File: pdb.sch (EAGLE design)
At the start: 42 parts, among them Q1 20MHz, Q2 IRFR5305PBF, Q3 IRFR5305PBF, U1 TSR_1-2433, U2 LTC2946CMSPBF, U3 LTC2946CMSPBF, U4 LTC2946CMSPBF, U5 ATMEGA48-20AU, U6 TXB0104, U7 AT30TS74SS8M

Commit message: wip
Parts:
- removed BAT: XT60PWMALE, amass:XT60PWMALE
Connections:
- removed net N$3: BAT.+, Q2.D
- new net BAT_IN: Q2.D
- net GND: no longer BAT.-
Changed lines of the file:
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@@
 <part name="U1" library="Robo-Lib" deviceset="TSR_1-*" device="" technology="2433"/>
 <part name="SUPPLY6" library="supply2" library_urn="urn:adsk.eagle:library:372" deviceset="V+" device=""/>
-<part name="BAT" library="amass" library_urn="urn:adsk.eagle:library:538876" deviceset="XT60PW" device="MALE" package3d_urn="urn:adsk.eagle:package:538884/2"/>
 <part name="LED1" library="led" library_urn="urn:adsk.eagle:library:259" deviceset="LED" device="CHIP-LED0603" package3d_urn="urn:adsk.eagle:package:15819/3" value="blau"/>
 <part name="LED2" library="led" library_urn="urn:adsk.eagle:library:259" deviceset="LED" device="CHIP-LED0603" package3d_urn="urn:adsk.eagle:package:15819/3" value="grün"/>
@@
 <instance part="U1" gate="G$1" x="2.54" y="15.24"/>
 <instance part="SUPPLY6" gate="1" x="-12.7" y="20.32"/>
-<instance part="BAT" gate="G$1" x="-99.06" y="53.34" rot="MR0"/>
 <instance part="R4" gate="G$1" x="-27.94" y="55.88"/>
 <instance part="R5" gate="G$1" x="25.4" y="55.88"/>
@@
 <wire x1="-81.28" y1="50.8" x2="-81.28" y2="48.26" width="0.1524" layer="91"/>
 <pinref part="GND25" gate="1" pin="GND"/>
-<pinref part="BAT" gate="G$1" pin="-"/>
 </segment>
 <segment>
@@
 </segment>
 </net>
-<net name="AKKU-ZWISCHEN" class="2">
+<net name="AKKU-ZWISCHEN" class="1">
 <segment>
 <pinref part="Q2" gate="G$1" pin="S"/>
@@
 </segment>
 </net>
-<net name="N$3" class="0">
+<net name="BAT_IN" class="1">
 <segment>
 <pinref part="Q2" gate="G$1" pin="D"/>
 <wire x1="-88.9" y1="55.88" x2="-78.74" y2="55.88" width="0.1524" layer="91"/>
-<pinref part="BAT" gate="G$1" pin="+"/>
 </segment>
 </net>
@@
 </segment>
 </net>
-<net name="SENSE+V+" class="3">
+<net name="SENSE+V+" class="4">
 <segment>
 <pinref part="Q3" gate="G$1" pin="D"/>
@@
 </segment>
 </net>
-<net name="SENSE+V+" class="3">
+<net name="SENSE+V+" class="4">
 <segment>
 <pinref part="U2" gate="A" pin="SENSE+"/>

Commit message: changed R6
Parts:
- R6: value CSS2H-3920 -> CRA2512-FZ-R040ELF; device jonas_resistor:CSS2H-3920 -> jonas_bourns:CRA2512-FZ-R040ELF
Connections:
- net +3V3: now also R6.22; no longer R6.2
- net SENSE+3V3: now also R6.11; no longer R6.1
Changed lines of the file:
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@@
 <?xml version="1.0" encoding="utf-8"?>
 <!DOCTYPE eagle SYSTEM "eagle.dtd">
-<eagle version="8.5.2">
+<eagle version="8.6.0">
 <drawing>
 <settings>
@@
 <part name="R4" library="jonas_resistor" library_urn="urn:adsk.eagle:library:539632" deviceset="CSS2H-3920" device="" package3d_urn="urn:adsk.eagle:package:539635/1"/>
 <part name="R5" library="jonas_resistor" library_urn="urn:adsk.eagle:library:539632" deviceset="CSS2H-3920" device="" package3d_urn="urn:adsk.eagle:package:539635/1"/>
-<part name="R6" library="jonas_resistor" library_urn="urn:adsk.eagle:library:539632" deviceset="CSS2H-3920" device="" package3d_urn="urn:adsk.eagle:package:539635/1"/>
 <part name="+3V3" library="supply1" library_urn="urn:adsk.eagle:library:371" deviceset="+3V3" device=""/>
 <part name="SUPPLY12" library="supply2" library_urn="urn:adsk.eagle:library:372" deviceset="+5V" device=""/>
@@
 <part name="GND22" library="supply1" library_urn="urn:adsk.eagle:library:371" deviceset="GND" device=""/>
 <part name="SUPPLY21" library="supply2" deviceset="+5V" device=""/>
+<part name="R6" library="jonas_bourns" library_urn="urn:adsk.eagle:library:1422904" deviceset="CRA2512-FZ-R040ELF" device="" package3d_urn="urn:adsk.eagle:package:1633525/2"/>
 </parts>
 <sheets>
@@
 <instance part="GND19" gate="1" x="38.1" y="0"/>
 <instance part="GND15" gate="1" x="15.24" y="2.54"/>
-<instance part="+3V2" gate="G$1" x="53.34" y="20.32"/>
+<instance part="+3V2" gate="G$1" x="58.42" y="20.32"/>
 <instance part="U1" gate="G$1" x="2.54" y="15.24"/>
 <instance part="SUPPLY6" gate="1" x="-12.7" y="20.32"/>
 <instance part="R4" gate="G$1" x="-27.94" y="55.88"/>
 <instance part="R5" gate="G$1" x="25.4" y="55.88"/>
-<instance part="R6" gate="G$1" x="45.72" y="15.24"/>
 <instance part="FRAME3" gate="G$1" x="-127" y="-50.8"/>
 <instance part="ESC" gate="G$1" x="-99.06" y="-17.78" rot="MR0"/>
@@
 <instance part="SUPPLY17" gate="1" x="-86.36" y="-10.16"/>
 <instance part="L2" gate="A" x="20.32" y="15.24"/>
+<instance part="R6" gate="A" x="43.18" y="15.24"/>
 </instances>
 <busses>
@@
 <wire x1="38.1" y1="15.24" x2="38.1" y2="12.7" width="0.1524" layer="91"/>
 <pinref part="C4" gate="G$1" pin="1"/>
-<pinref part="R6" gate="G$1" pin="1"/>
-<wire x1="38.1" y1="15.24" x2="40.64" y2="15.24" width="0.1524" layer="91"/>
+<wire x1="38.1" y1="15.24" x2="43.18" y2="15.24" width="0.1524" layer="91"/>
 <wire x1="35.56" y1="15.24" x2="38.1" y2="15.24" width="0.1524" layer="91"/>
 <junction x="38.1" y="15.24"/>
@@
 <label x="38.1" y="17.78" size="1.778" layer="95" rot="R90" xref="yes"/>
 <pinref part="L2" gate="A" pin="1"/>
+<pinref part="R6" gate="A" pin="11"/>
 </segment>
 </net>
 <net name="+3V3" class="4">
 <segment>
-<pinref part="R6" gate="G$1" pin="2"/>
-<wire x1="50.8" y1="15.24" x2="53.34" y2="15.24" width="0.1524" layer="91"/>
-<wire x1="53.34" y1="15.24" x2="53.34" y2="17.78" width="0.1524" layer="91"/>
+<wire x1="55.88" y1="15.24" x2="58.42" y2="15.24" width="0.1524" layer="91"/>
+<wire x1="58.42" y1="15.24" x2="58.42" y2="17.78" width="0.1524" layer="91"/>
 <pinref part="+3V2" gate="G$1" pin="+3V3"/>
-</segment>
-</net>
+<pinref part="R6" gate="A" pin="22"/>
+</segment>
+</net>

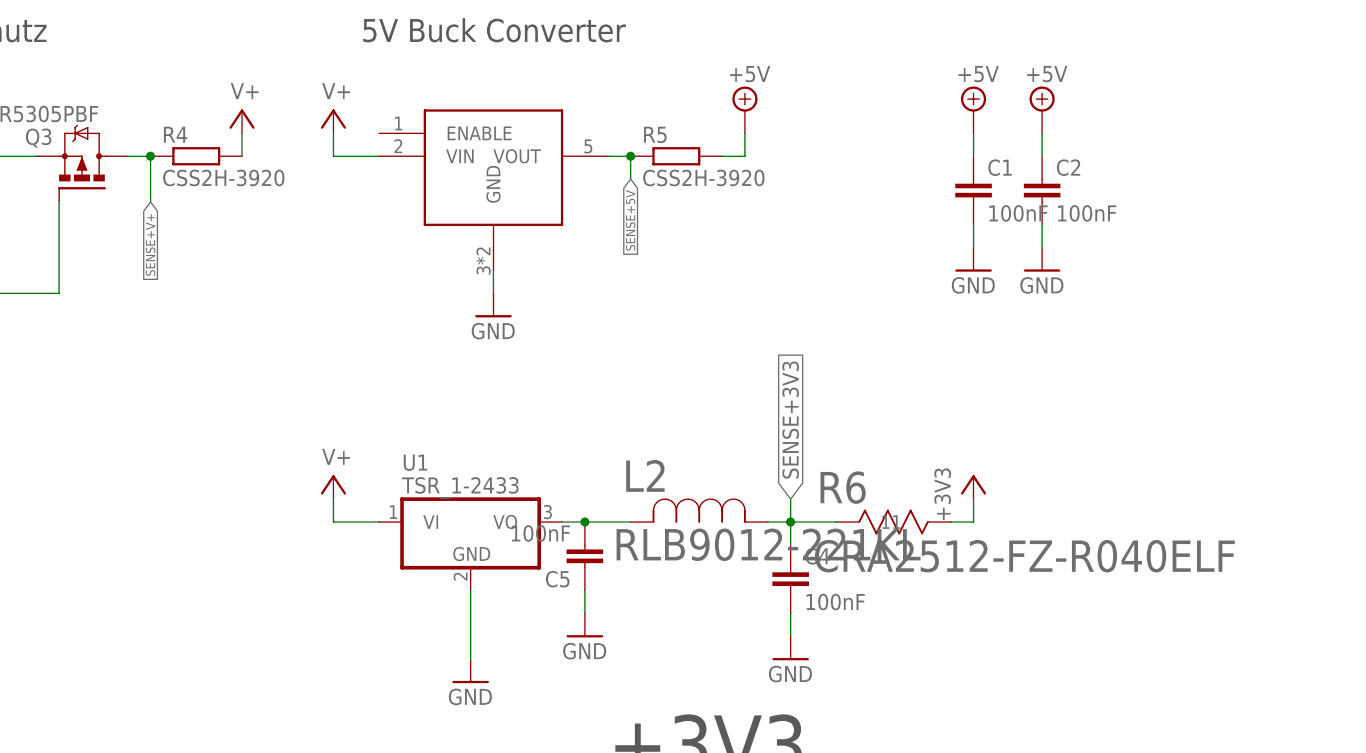
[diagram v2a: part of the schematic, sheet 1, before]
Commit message: fixed shunt resistor libraries
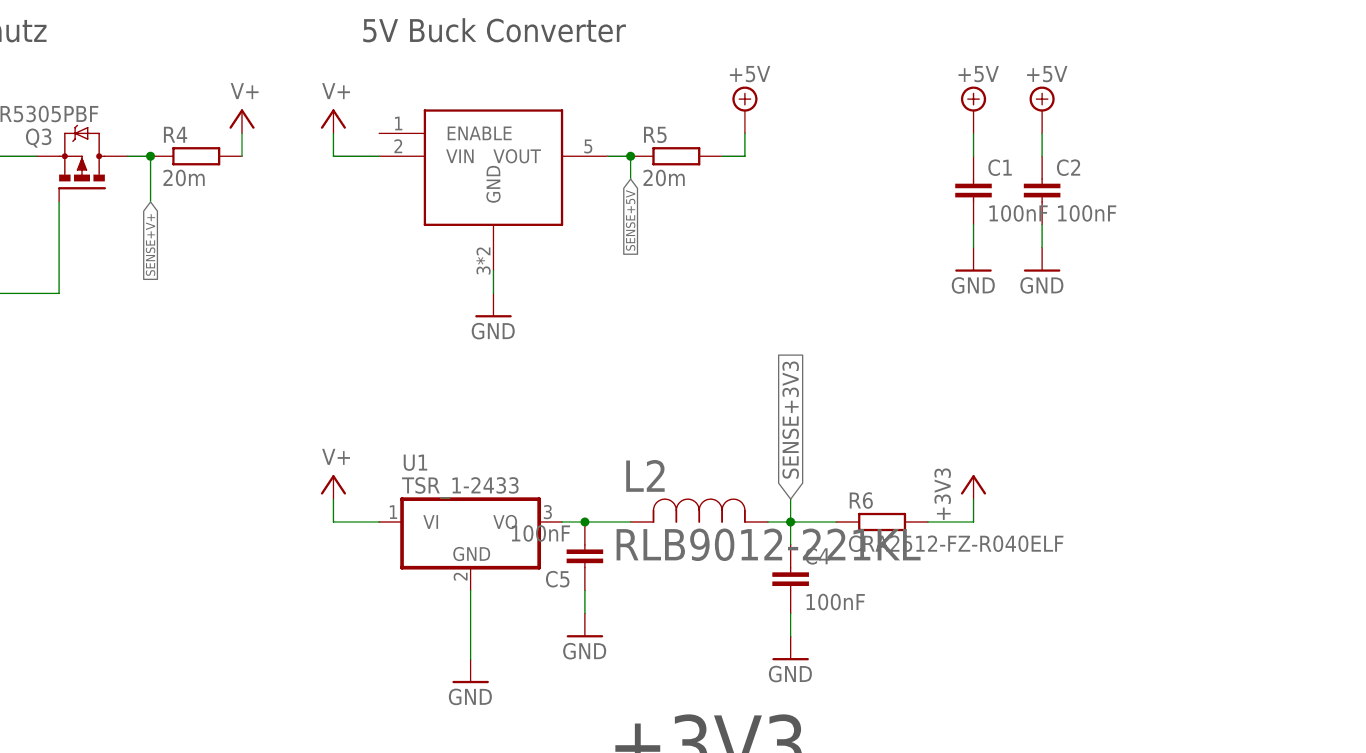
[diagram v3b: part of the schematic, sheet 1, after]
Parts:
- R4, R5: value CSS2H-3920 -> 20m
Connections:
- net +3V3: now also R6.2; no longer R6.22
- net SENSE+3V3: now also R6.1; no longer R6.11
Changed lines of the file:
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@@
 <layer number="97" name="Info" color="7" fill="1" visible="yes" active="yes"/>
 <layer number="98" name="Guide" color="6" fill="1" visible="yes" active="yes"/>
-<layer number="99" name="SpiceOrder" color="7" fill="1" visible="yes" active="yes"/>
+<layer number="99" name="SpiceOrder" color="7" fill="1" visible="no" active="yes"/>
 <layer number="100" name="Muster" color="7" fill="1" visible="no" active="no"/>
 <layer number="101" name="Hidden" color="15" fill="1" visible="yes" active="yes"/>
@@
 <part name="SUPPLY10" library="supply2" library_urn="urn:adsk.eagle:library:372" deviceset="V+" device=""/>
 <part name="SUPPLY11" library="supply2" library_urn="urn:adsk.eagle:library:372" deviceset="V+" device=""/>
-<part name="R4" library="jonas_resistor" library_urn="urn:adsk.eagle:library:539632" deviceset="CSS2H-3920" device="" package3d_urn="urn:adsk.eagle:package:539635/1"/>
-<part name="R5" library="jonas_resistor" library_urn="urn:adsk.eagle:library:539632" deviceset="CSS2H-3920" device="" package3d_urn="urn:adsk.eagle:package:539635/1"/>
+<part name="R4" library="jonas_resistor" library_urn="urn:adsk.eagle:library:539632" deviceset="CSS2H-3920" device="" package3d_urn="urn:adsk.eagle:package:539635/1" value="20m"/>
+<part name="R5" library="jonas_resistor" library_urn="urn:adsk.eagle:library:539632" deviceset="CSS2H-3920" device="" package3d_urn="urn:adsk.eagle:package:539635/1" value="20m"/>
 <part name="+3V3" library="supply1" library_urn="urn:adsk.eagle:library:371" deviceset="+3V3" device=""/>
 <part name="SUPPLY12" library="supply2" library_urn="urn:adsk.eagle:library:372" deviceset="+5V" device=""/>
@@
 <instance part="SUPPLY17" gate="1" x="-86.36" y="-10.16"/>
 <instance part="L2" gate="A" x="20.32" y="15.24"/>
-<instance part="R6" gate="A" x="43.18" y="15.24"/>
+<instance part="R6" gate="G$1" x="48.26" y="15.24"/>
 </instances>
 <busses>
@@
 <wire x1="38.1" y1="15.24" x2="38.1" y2="12.7" width="0.1524" layer="91"/>
 <pinref part="C4" gate="G$1" pin="1"/>
-<wire x1="38.1" y1="15.24" x2="43.18" y2="15.24" width="0.1524" layer="91"/>
 <wire x1="35.56" y1="15.24" x2="38.1" y2="15.24" width="0.1524" layer="91"/>
 <junction x="38.1" y="15.24"/>
@@
 <label x="38.1" y="17.78" size="1.778" layer="95" rot="R90" xref="yes"/>
 <pinref part="L2" gate="A" pin="1"/>
-<pinref part="R6" gate="A" pin="11"/>
+<pinref part="R6" gate="G$1" pin="1"/>
+<wire x1="38.1" y1="15.24" x2="43.18" y2="15.24" width="0.1524" layer="91"/>
 </segment>
 </net>
 <net name="+3V3" class="4">
 <segment>
-<wire x1="55.88" y1="15.24" x2="58.42" y2="15.24" width="0.1524" layer="91"/>
 <wire x1="58.42" y1="15.24" x2="58.42" y2="17.78" width="0.1524" layer="91"/>
 <pinref part="+3V2" gate="G$1" pin="+3V3"/>
-<pinref part="R6" gate="A" pin="22"/>
-</segment>
-</net>
+<pinref part="R6" gate="G$1" pin="2"/>
+<wire x1="53.34" y1="15.24" x2="58.42" y2="15.24" width="0.1524" layer="91"/>
+</segment>
+</net>

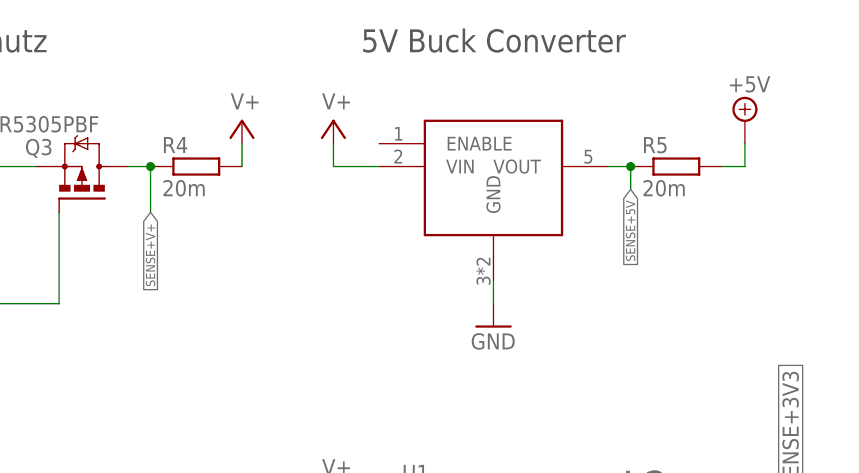
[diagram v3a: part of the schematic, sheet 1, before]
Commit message: fixed shunt resistor value
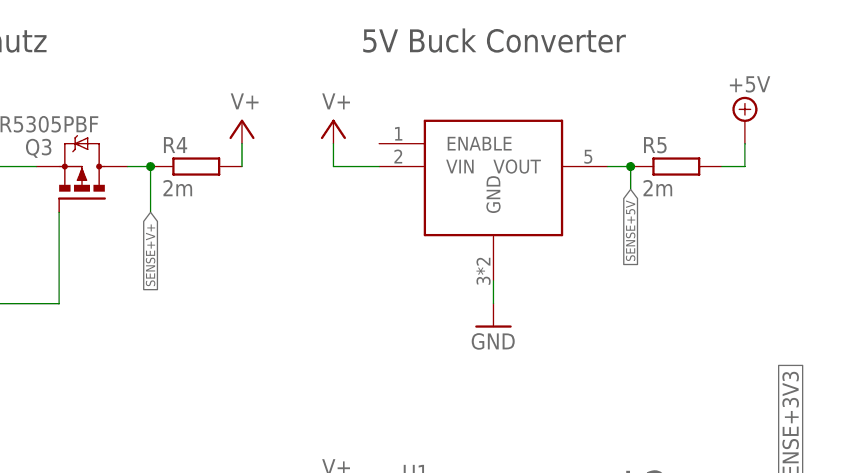
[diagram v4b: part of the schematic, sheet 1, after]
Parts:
- R4, R5: value 20m -> 2m
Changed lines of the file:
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@@
 <part name="SUPPLY10" library="supply2" library_urn="urn:adsk.eagle:library:372" deviceset="V+" device=""/>
 <part name="SUPPLY11" library="supply2" library_urn="urn:adsk.eagle:library:372" deviceset="V+" device=""/>
-<part name="R4" library="jonas_resistor" library_urn="urn:adsk.eagle:library:539632" deviceset="CSS2H-3920" device="" package3d_urn="urn:adsk.eagle:package:539635/1" value="20m"/>
-<part name="R5" library="jonas_resistor" library_urn="urn:adsk.eagle:library:539632" deviceset="CSS2H-3920" device="" package3d_urn="urn:adsk.eagle:package:539635/1" value="20m"/>
+<part name="R4" library="jonas_resistor" library_urn="urn:adsk.eagle:library:539632" deviceset="CSS2H-3920" device="" package3d_urn="urn:adsk.eagle:package:539635/1" value="2m"/>
+<part name="R5" library="jonas_resistor" library_urn="urn:adsk.eagle:library:539632" deviceset="CSS2H-3920" device="" package3d_urn="urn:adsk.eagle:package:539635/1" value="2m"/>
 <part name="+3V3" library="supply1" library_urn="urn:adsk.eagle:library:371" deviceset="+3V3" device=""/>
 <part name="SUPPLY12" library="supply2" library_urn="urn:adsk.eagle:library:372" deviceset="+5V" device=""/>

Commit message: various improvements/fixes
added power output pins
fixed design rules
moved ESC out to bottom
fixed packages
removed unnecessary filtering for atmega
etc
(may be more but that was last week i don't remember anymore)
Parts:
- removed C10: 100nF, resistor:C-EUC1206
- removed L1: 100µH, rcl:L-EU0204/7
- added JP10, JP2, JP3, JP4, JP5, JP6, JP7, JP8, JP9: (no value), pinhead:PINHD-1X2
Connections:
- removed net N$88: C10.2, L1.1, U5B.AVCC
- net +3V3: now also JP10.1, JP8.1, JP9.1
- net +5V: now also JP5.1, JP6.1, JP7.1, U5B.AVCC; no longer L1.2
- net GND: now also JP10.2, JP2.2, JP3.2, JP4.2, JP5.2, JP6.2, JP7.2, JP8.2, JP9.2; no longer C10.1
- net V+: now also JP2.1, JP3.1, JP4.1
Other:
- note removed: "TODO: Replace with SMT package"

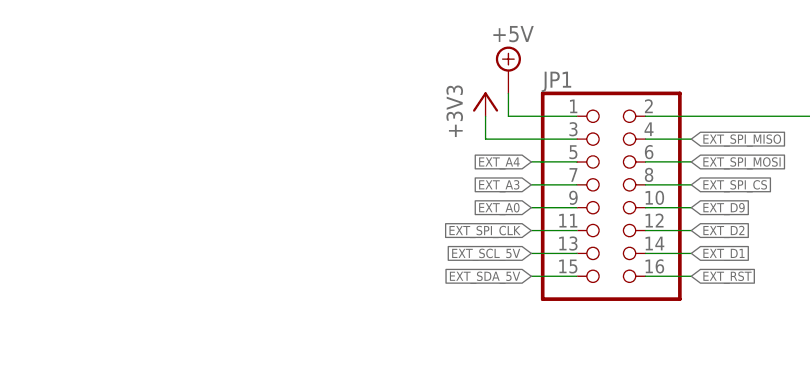
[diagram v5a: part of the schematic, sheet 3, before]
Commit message: fixed #10
removed expansion port connections
rotated expansion port
connected expansion port
added 3V3 jumper
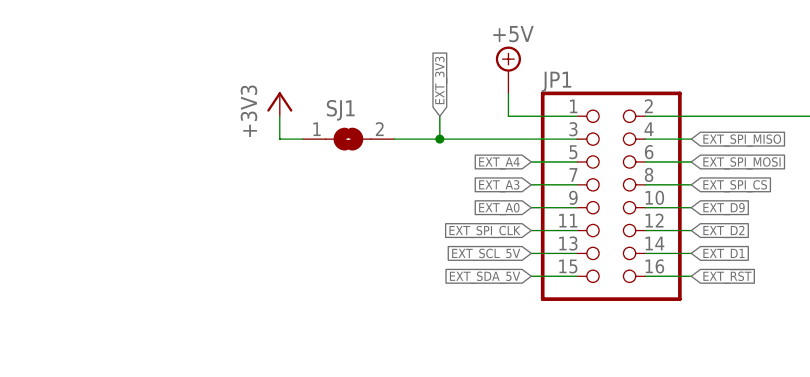
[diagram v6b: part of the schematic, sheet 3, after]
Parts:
- added SJ1: (no value), jumper:SJ
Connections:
- new net EXT_3V3: JP1.3, SJ1.2, U6.VCCA
- net +3V3: now also SJ1.1; no longer JP1.3, U6.VCCA
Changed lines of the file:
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@@
 <part name="SUPPLY16" library="supply2" deviceset="+5V" device=""/>
 <part name="GND16" library="supply1" deviceset="GND" device=""/>
-<part name="+3V4" library="supply1" library_urn="urn:adsk.eagle:library:371" deviceset="+3V3" device=""/>
 <part name="ESC" library="amass" library_urn="urn:adsk.eagle:library:538876" deviceset="XT60PW" device="FEMALE" package3d_urn="urn:adsk.eagle:package:538883/2" value="XT60PWFEMALE"/>
 <part name="GND18" library="supply1" deviceset="GND" device=""/>
@@
 <part name="GND21" library="supply1" library_urn="urn:adsk.eagle:library:371" deviceset="GND" device=""/>
 <part name="SUPPLY19" library="supply2" library_urn="urn:adsk.eagle:library:372" deviceset="+5V" device=""/>
-<part name="+3V5" library="supply1" library_urn="urn:adsk.eagle:library:371" deviceset="+3V3" device=""/>
 <part name="R7" library="rcl" library_urn="urn:adsk.eagle:library:334" deviceset="R-EU_" device="R0805" package3d_urn="urn:adsk.eagle:package:23553/2" value="4,7k"/>
 <part name="R8" library="rcl" library_urn="urn:adsk.eagle:library:334" deviceset="R-EU_" device="R0805" package3d_urn="urn:adsk.eagle:package:23553/2" value="4,7k"/>
@@
 <part name="SUPPLY22" library="supply2" library_urn="urn:adsk.eagle:library:372" deviceset="+5V" device=""/>
 <part name="+3V6" library="supply1" library_urn="urn:adsk.eagle:library:371" deviceset="+3V3" device=""/>
+<part name="SJ1" library="jumper" library_urn="urn:adsk.eagle:library:252" deviceset="SJ" device="" package3d_urn="urn:adsk.eagle:package:15471/1"/>
+<part name="+3V4" library="supply1" library_urn="urn:adsk.eagle:library:371" deviceset="+3V3" device=""/>
 </parts>
 <sheets>
@@
 <instance part="SUPPLY16" gate="+5V" x="45.72" y="106.68"/>
 <instance part="GND16" gate="1" x="40.64" y="63.5"/>
-<instance part="+3V4" gate="G$1" x="35.56" y="106.68"/>
 <instance part="R7" gate="G$1" x="66.04" y="76.2" rot="R180"/>
 <instance part="R8" gate="G$1" x="66.04" y="83.82" rot="R180"/>
@@
 <wire x1="50.8" y1="149.86" x2="50.8" y2="147.32" width="0.1524" layer="91"/>
 </segment>
-<segment>
-<pinref part="U6" gate="G$1" pin="VCCA"/>
-<wire x1="35.56" y1="101.6" x2="35.56" y2="104.14" width="0.1524" layer="91"/>
-<pinref part="+3V4" gate="G$1" pin="+3V3"/>
-</segment>
 </net>
 <net name="+5V" class="4">
@@
 <wire x1="55.88" y1="81.28" x2="60.96" y2="81.28" width="0.1524" layer="91"/>
 <wire x1="60.96" y1="81.28" x2="60.96" y2="76.2" width="0.1524" layer="91"/>
+</segment>
+</net>
+<net name="EXT_3V3" class="4">
+<segment>
+<pinref part="U6" gate="G$1" pin="VCCA"/>
+<wire x1="35.56" y1="101.6" x2="35.56" y2="104.14" width="0.1524" layer="91"/>
+<label x="35.56" y="104.14" size="1.016" layer="95" rot="R90" xref="yes"/>
 </segment>
 </net>
@@
 <instance part="GND21" gate="1" x="180.34" y="213.36"/>
 <instance part="SUPPLY19" gate="+5V" x="142.24" y="223.52"/>
-<instance part="+3V5" gate="G$1" x="139.7" y="220.98"/>
+<instance part="SJ1" gate="1" x="124.46" y="215.9"/>
+<instance part="+3V4" gate="G$1" x="116.84" y="220.98"/>
 </instances>
 <busses>
@@
 </segment>
 <segment>
-<pinref part="JP1" gate="A" pin="3"/>
-<wire x1="149.86" y1="215.9" x2="139.7" y2="215.9" width="0.1524" layer="91"/>
-<wire x1="139.7" y1="215.9" x2="139.7" y2="218.44" width="0.1524" layer="91"/>
-<pinref part="+3V5" gate="G$1" pin="+3V3"/>
+<pinref part="SJ1" gate="1" pin="1"/>
+<pinref part="+3V4" gate="G$1" pin="+3V3"/>
+<wire x1="119.38" y1="215.9" x2="116.84" y2="215.9" width="0.1524" layer="91"/>
+<wire x1="116.84" y1="215.9" x2="116.84" y2="218.44" width="0.1524" layer="91"/>
 </segment>
 </net>
@@
 </segment>
 </net>
+<net name="EXT_3V3" class="4">
+<segment>
+<pinref part="JP1" gate="A" pin="3"/>
+<label x="134.62" y="218.44" size="1.016" layer="95" rot="R90" xref="yes"/>
+<pinref part="SJ1" gate="1" pin="2"/>
+<wire x1="149.86" y1="215.9" x2="134.62" y2="215.9" width="0.1524" layer="91"/>
+<wire x1="134.62" y1="215.9" x2="129.54" y2="215.9" width="0.1524" layer="91"/>
+<wire x1="134.62" y1="218.44" x2="134.62" y2="215.9" width="0.1524" layer="91"/>
+<junction x="134.62" y="215.9"/>
+</segment>
+</net>
